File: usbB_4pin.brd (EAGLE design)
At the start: 100 x 80 mm, 12 parts, among them IC1 788TV, IC2 TINY13-20PU, X1 PN61729-S

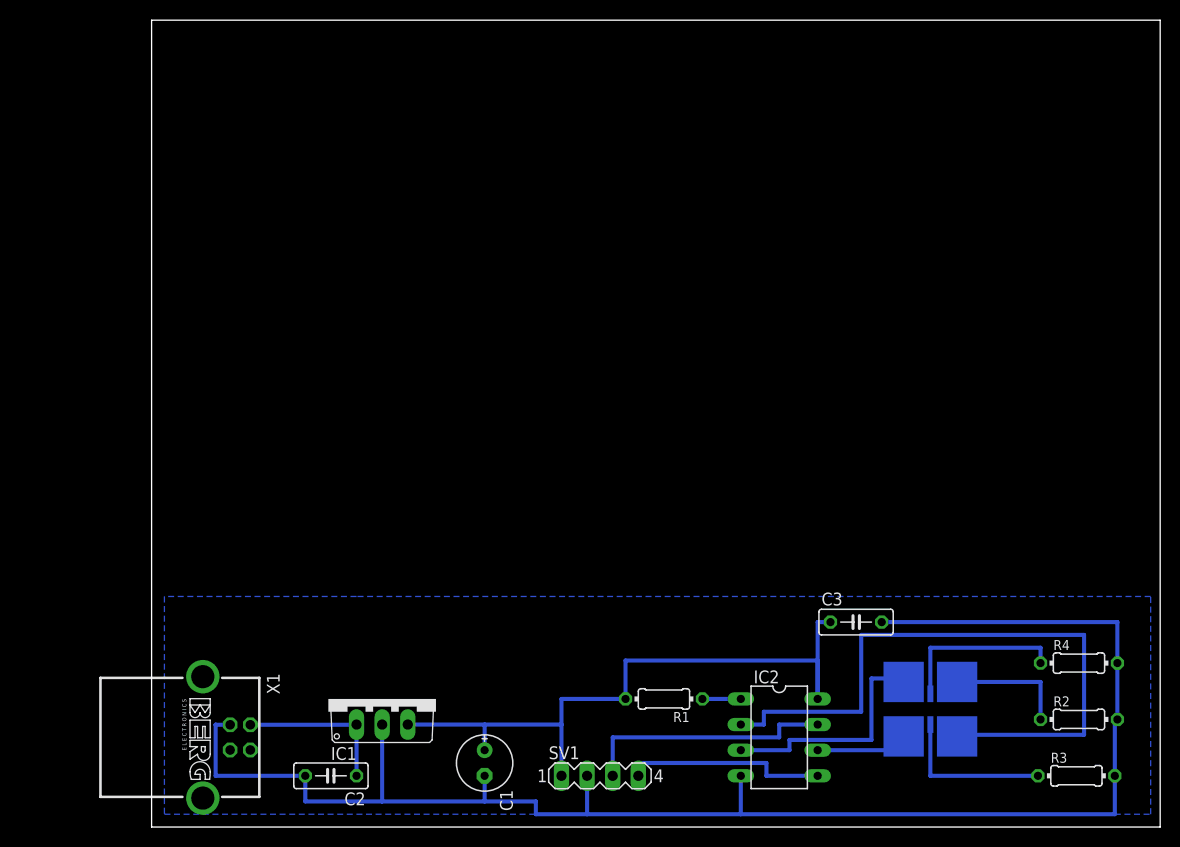
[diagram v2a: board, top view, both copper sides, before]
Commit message: correct pin headers ftw
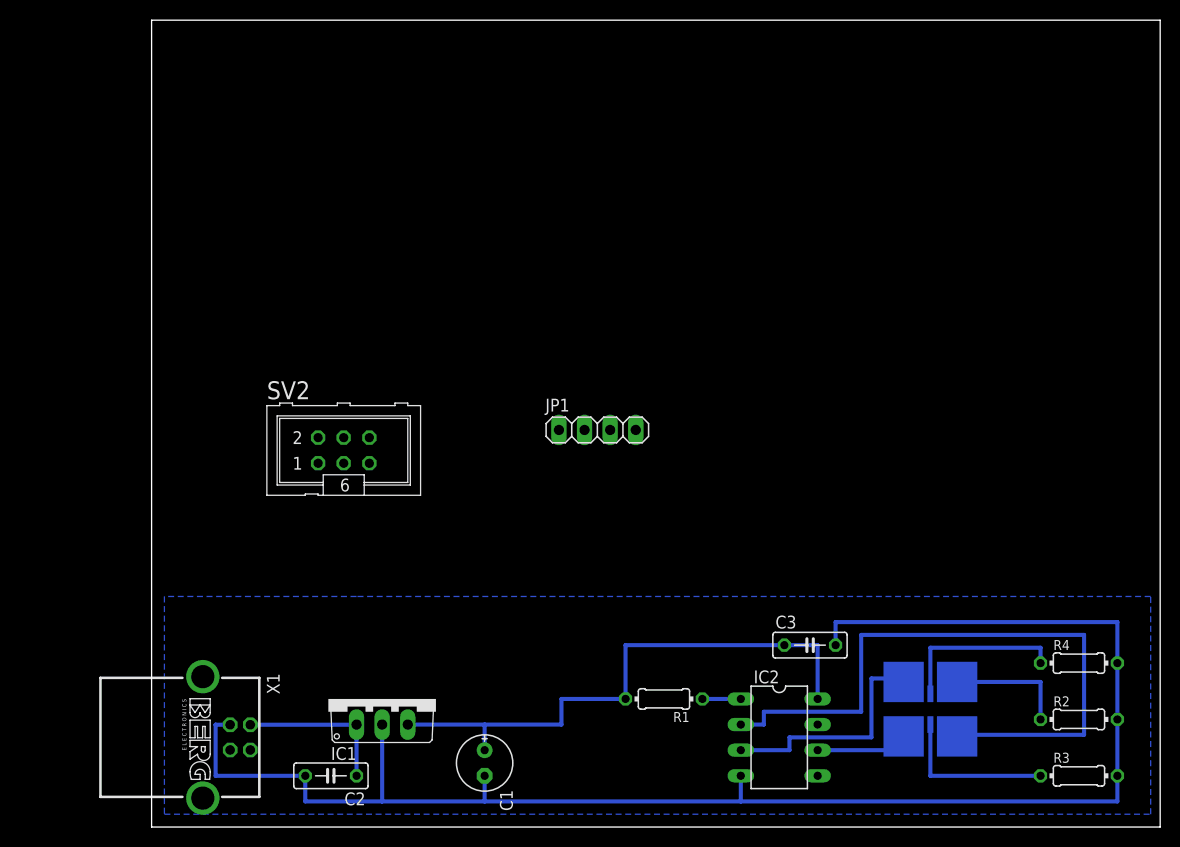
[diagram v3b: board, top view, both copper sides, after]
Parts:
- removed SV1: (no value), con-lstb:MA04-1
- added JP1: (no value), pinhead:1X04
- added SV2: PROG, con-ml:ML6
- moved C3 5.11 mm to (65.3, 18.0)
- moved R3 0.25 mm to (91.9, 5.08)
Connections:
- removed net N$12: IC2.5
- removed net N$13: IC2.7, SV1.3
- removed net N$4: IC2.1, R1.1
- removed net N$5: IC2.6, LED1.3
- new net MISO: IC2.6, LED1.3, SV2.1
- new net N$10: IC2.5, JP1.3, SV2.4
- new net SCK: IC2.7, JP1.4, SV2.3
- new net _RESET: IC2.1, R1.1, SV2.5
- net GND: now also JP1.2, SV2.6; no longer SV1.2
- net VCC: now also JP1.1, SV2.2; no longer SV1.1
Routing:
- net N$13: track 25.4 -> 0.00 mm
- net N$12: track 19.1 -> 0.00 mm
- net VCC: track 67.3 -> 56.4 mm
- net N$5: track 9.89 -> 0.00 mm
- net MISO: track 0.00 -> 9.89 mm
- net _RESET: track 0.00 -> 3.81 mm
- net N$4: track 3.81 -> 0.00 mm
- net GND: track 159.9 -> 159.2 mm
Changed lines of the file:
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@@
 <element name="C1" library="rcl" package="E2,5-6E" value="33u" x="33.02" y="6.35" rot="R270"/>
 <element name="C2" library="rcl" package="C050-025X075" value="470n" x="17.78" y="5.08" rot="R180"/>
-<element name="C3" library="rcl" package="C050-025X075" value="100n" x="69.85" y="20.32"/>
+<element name="C3" library="rcl" package="C050-025X075" value="100n" x="65.278" y="18.034"/>
 <element name="R1" library="resistor" package="0204/7" value="10k" x="50.8" y="12.7" rot="R180"/>
 <element name="R2" library="resistor" package="0204/7" value="150" x="91.948" y="10.668"/>
-<element name="R3" library="resistor" package="0204/7" value="91" x="91.694" y="5.08"/>
+<element name="R3" library="resistor" package="0204/7" value="91" x="91.948" y="5.08"/>
 <element name="R4" library="resistor" package="0204/7" value="91" x="91.948" y="16.256"/>
 <element name="IC1" library="linear" package="TO220V" value="788TV" x="22.86" y="12.7"/>
@@
 </element>
 <element name="LED1" library="led" package="LRTB_G6SG" value="LRTB_G6SG" x="77.216" y="11.684" rot="SMR0"/>
-<element name="SV1" library="con-lstb" package="MA04-1" value="" x="44.45" y="5.08">
-<attribute name="OC_NEWARK" value="unknown" x="73.66" y="-29.21" size="1.778" layer="27" display="off"/>
-<attribute name="MPN" value="" x="73.66" y="-29.21" size="1.778" layer="27" display="off"/>
-<attribute name="MF" value="" x="73.66" y="-29.21" size="1.778" layer="27" display="off"/>
-<attribute name="OC_FARNELL" value="unknown" x="73.66" y="-29.21" size="1.778" layer="27" display="off"/>
-</element>
 <element name="X1" library="con-berg" package="PN61729-S" value="PN61729-S" x="5.08" y="8.89" rot="R270">
 <attribute name="OC_NEWARK" value="unknown" x="-6.35" y="-12.7" size="1.778" layer="27" rot="R270" display="off"/>
@@
 <attribute name="OC_FARNELL" value="unknown" x="-6.35" y="-12.7" size="1.778" layer="27" rot="R270" display="off"/>
 </element>
+<element name="SV2" library="con-ml" package="ML6" value="PROG" x="19.05" y="37.338">
+<attribute name="OC_NEWARK" value="unknown" x="19.05" y="37.338" size="1.778" layer="27" display="off"/>
+<attribute name="MPN" value="" x="19.05" y="37.338" size="1.778" layer="27" display="off"/>
+<attribute name="MF" value="" x="19.05" y="37.338" size="1.778" layer="27" display="off"/>
+<attribute name="OC_FARNELL" value="unknown" x="19.05" y="37.338" size="1.778" layer="27" display="off"/>
+</element>
+<element name="JP1" library="pinhead" package="1X04" value="" x="44.196" y="39.37"/>
 </elements>
 <signals>
@@
 <contactref element="C1" pad="-"/>
 <contactref element="IC2" pad="4"/>
-<contactref element="SV1" pad="2"/>
 <contactref element="C3" pad="2"/>
 <contactref element="R2" pad="2"/>
@@
 <wire x1="22.86" y1="2.54" x2="33.02" y2="2.54" width="0.4064" layer="16"/>
 <wire x1="33.02" y1="5.08" x2="33.02" y2="2.54" width="0.4064" layer="16"/>
-<wire x1="33.02" y1="2.54" x2="38.1" y2="2.54" width="0.4064" layer="16"/>
-<wire x1="38.1" y1="2.54" x2="38.1" y2="1.27" width="0.4064" layer="16"/>
-<wire x1="38.1" y1="1.27" x2="43.18" y2="1.27" width="0.4064" layer="16"/>
-<wire x1="95.504" y1="1.27" x2="58.42" y2="1.27" width="0.4064" layer="16"/>
-<wire x1="58.42" y1="1.27" x2="58.42" y2="5.08" width="0.4064" layer="16"/>
-<wire x1="43.18" y1="5.08" x2="43.18" y2="1.27" width="0.4064" layer="16"/>
-<wire x1="43.18" y1="1.27" x2="58.42" y2="1.27" width="0.4064" layer="16"/>
-<wire x1="95.504" y1="5.08" x2="95.504" y2="1.27" width="0.4064" layer="16"/>
-<wire x1="72.39" y1="20.32" x2="95.758" y2="20.32" width="0.4064" layer="16"/>
+<wire x1="95.758" y1="2.54" x2="58.42" y2="2.54" width="0.4064" layer="16"/>
+<wire x1="58.42" y1="2.54" x2="58.42" y2="5.08" width="0.4064" layer="16"/>
+<wire x1="33.02" y1="2.54" x2="58.42" y2="2.54" width="0.4064" layer="16"/>
+<wire x1="95.758" y1="5.08" x2="95.758" y2="2.54" width="0.4064" layer="16"/>
+<wire x1="67.818" y1="18.034" x2="67.818" y2="20.32" width="0.4064" layer="16"/>
+<wire x1="67.818" y1="20.32" x2="95.758" y2="20.32" width="0.4064" layer="16"/>
 <wire x1="95.758" y1="20.32" x2="95.758" y2="16.256" width="0.4064" layer="16"/>
 <wire x1="95.758" y1="16.256" x2="95.758" y2="10.668" width="0.4064" layer="16"/>
-<wire x1="95.758" y1="10.668" x2="95.504" y2="10.668" width="0.4064" layer="16"/>
-<wire x1="95.504" y1="10.668" x2="95.504" y2="5.08" width="0.4064" layer="16"/>
+<wire x1="95.758" y1="10.668" x2="95.758" y2="5.08" width="0.4064" layer="16"/>
+<contactref element="JP1" pad="2"/>
+<contactref element="SV2" pad="6"/>
+<wire x1="21.59" y1="38.608" x2="42.926" y2="39.37" width="0" layer="19" extent="1-1"/>
+<wire x1="22.86" y1="10.16" x2="21.59" y2="38.608" width="0" layer="19" extent="1-1"/>
 </signal>
 <signal name="VCC">
@@
 <contactref element="R1" pad="2"/>
 <contactref element="IC2" pad="8"/>
-<contactref element="SV1" pad="1"/>
 <contactref element="C3" pad="1"/>
 <wire x1="25.4" y1="10.16" x2="33.02" y2="10.16" width="0.4064" layer="16"/>
 <wire x1="33.02" y1="7.62" x2="33.02" y2="10.16" width="0.4064" layer="16"/>
 <wire x1="33.02" y1="10.16" x2="40.64" y2="10.16" width="0.4064" layer="16"/>
-<wire x1="40.64" y1="10.16" x2="40.64" y2="5.08" width="0.4064" layer="16"/>
 <wire x1="46.99" y1="12.7" x2="40.64" y2="12.7" width="0.4064" layer="16"/>
 <wire x1="40.64" y1="12.7" x2="40.64" y2="10.16" width="0.4064" layer="16"/>
-<wire x1="46.99" y1="12.7" x2="46.99" y2="16.51" width="0.4064" layer="16"/>
-<wire x1="46.99" y1="16.51" x2="66.04" y2="16.51" width="0.4064" layer="16"/>
-<wire x1="66.04" y1="16.51" x2="66.04" y2="12.7" width="0.4064" layer="16"/>
-<wire x1="66.04" y1="12.7" x2="66.04" y2="20.32" width="0.4064" layer="16"/>
-<wire x1="66.04" y1="20.32" x2="67.31" y2="20.32" width="0.4064" layer="16"/>
+<wire x1="46.99" y1="12.7" x2="46.99" y2="18.034" width="0.4064" layer="16"/>
+<wire x1="46.99" y1="18.034" x2="62.738" y2="18.034" width="0.4064" layer="16"/>
+<wire x1="62.738" y1="18.034" x2="66.04" y2="18.034" width="0.4064" layer="16"/>
+<wire x1="66.04" y1="18.034" x2="66.04" y2="12.7" width="0.4064" layer="16"/>
+<contactref element="JP1" pad="1"/>
+<contactref element="SV2" pad="2"/>
+<wire x1="46.99" y1="18.034" x2="40.386" y2="39.37" width="0" layer="19" extent="16-16"/>
+<wire x1="16.51" y1="38.608" x2="40.386" y2="39.37" width="0" layer="19" extent="1-1"/>
 </signal>
-<signal name="N$4">
+<signal name="_RESET">
 <contactref element="R1" pad="1"/>
 <contactref element="IC2" pad="1"/>
 <wire x1="58.42" y1="12.7" x2="54.61" y2="12.7" width="0.4064" layer="16"/>
+<contactref element="SV2" pad="5"/>
+<wire x1="21.59" y1="36.068" x2="54.61" y2="12.7" width="0" layer="19" extent="1-1"/>
 </signal>
 <signal name="N$6">
@@
 <contactref element="LED1" pad="2"/>
 <contactref element="R3" pad="1"/>
-<wire x1="87.884" y1="5.08" x2="77.216" y2="5.08" width="0.4064" layer="16"/>
+<wire x1="88.138" y1="5.08" x2="77.216" y2="5.08" width="0.4064" layer="16"/>
 <wire x1="77.216" y1="5.08" x2="77.216" y2="10.159" width="0.4064" layer="16"/>
 </signal>
@@
 <wire x1="79.866" y1="14.384" x2="88.138" y2="14.384" width="0.4064" layer="16"/>
 <wire x1="88.138" y1="14.384" x2="88.138" y2="10.668" width="0.4064" layer="16"/>
-</signal>
-<signal name="N$12">
-<contactref element="IC2" pad="5"/>
-<wire x1="66.04" y1="5.08" x2="60.96" y2="5.08" width="0.4064" layer="16"/>
-<wire x1="60.96" y1="5.08" x2="60.96" y2="6.35" width="0.4064" layer="16"/>
-<wire x1="60.96" y1="6.35" x2="48.26" y2="6.35" width="0.4064" layer="16"/>
-</signal>
-<signal name="N$13">
-<contactref element="IC2" pad="7"/>
-<contactref element="SV1" pad="3"/>
-<wire x1="45.72" y1="5.08" x2="45.72" y2="8.89" width="0.4064" layer="16"/>
-<wire x1="45.72" y1="8.89" x2="62.23" y2="8.89" width="0.4064" layer="16"/>
-<wire x1="62.23" y1="8.89" x2="62.23" y2="10.16" width="0.4064" layer="16"/>
-<wire x1="62.23" y1="10.16" x2="66.04" y2="10.16" width="0.4064" layer="16"/>
 </signal>
 <signal name="N$2">
@@
 <wire x1="79.866" y1="9.144" x2="79.866" y2="8.984" width="0.4064" layer="16"/>
 </signal>
-<signal name="N$5">
+<signal name="MISO">
 <contactref element="IC2" pad="6"/>
 <contactref element="LED1" pad="3"/>
 <wire x1="66.04" y1="7.62" x2="74.566" y2="7.62" width="0.4064" layer="16"/>
 <wire x1="74.566" y1="7.62" x2="74.566" y2="8.984" width="0.4064" layer="16"/>
+<contactref element="SV2" pad="1"/>
+<wire x1="16.51" y1="36.068" x2="66.04" y2="7.62" width="0" layer="19" extent="1-1"/>
 </signal>
 <signal name="N$9">
@@
 <contactref element="LED1" pad="4"/>
 <wire x1="58.42" y1="7.62" x2="63.246" y2="7.62" width="0.4064" layer="16"/>
-<wire x1="63.246" y1="7.62" x2="63.246" y2="8.636" width="0.4064" layer="16"/>
-<wire x1="63.246" y1="8.636" x2="71.374" y2="8.636" width="0.4064" layer="16"/>
-<wire x1="71.374" y1="8.636" x2="71.374" y2="14.732" width="0.4064" layer="16"/>
+<wire x1="63.246" y1="7.62" x2="63.246" y2="8.89" width="0.4064" layer="16"/>
+<wire x1="63.246" y1="8.89" x2="71.374" y2="8.89" width="0.4064" layer="16"/>
+<wire x1="71.374" y1="8.89" x2="71.374" y2="14.732" width="0.4064" layer="16"/>
 <wire x1="71.374" y1="14.732" x2="74.566" y2="14.732" width="0.4064" layer="16"/>
 <wire x1="74.566" y1="14.732" x2="74.566" y2="14.384" width="0.4064" layer="16"/>
 </signal>
+<signal name="N$10">
+<contactref element="JP1" pad="3"/>
+<contactref element="IC2" pad="5"/>
+<contactref element="SV2" pad="4"/>
+<wire x1="19.05" y1="38.608" x2="45.466" y2="39.37" width="0" layer="19" extent="1-1"/>
+<wire x1="66.04" y1="5.08" x2="45.466" y2="39.37" width="0" layer="19" extent="1-1"/>
+</signal>
+<signal name="SCK">
+<contactref element="JP1" pad="4"/>
+<contactref element="IC2" pad="7"/>
+<contactref element="SV2" pad="3"/>
+<wire x1="19.05" y1="36.068" x2="48.006" y2="39.37" width="0" layer="19" extent="1-1"/>
+<wire x1="66.04" y1="10.16" x2="48.006" y2="39.37" width="0" layer="19" extent="1-1"/>
+</signal>
 </signals>
